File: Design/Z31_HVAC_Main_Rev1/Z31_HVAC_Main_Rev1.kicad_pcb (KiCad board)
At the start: 2 copper layers, 179 x 133.5 mm, 22 parts, among them J2 Conn_02x18_Odd_Even, J3 Conn_01x10_Male, J4 Conn_01x09_Male, U1 MEGA2560PRO, U2 MCP2515, U3 TJR1443, U4 ULN2003, U5 ULN2003, U6 ULN2003, U7 ULN2003, U8 NCV4276B, U9 ULN2003

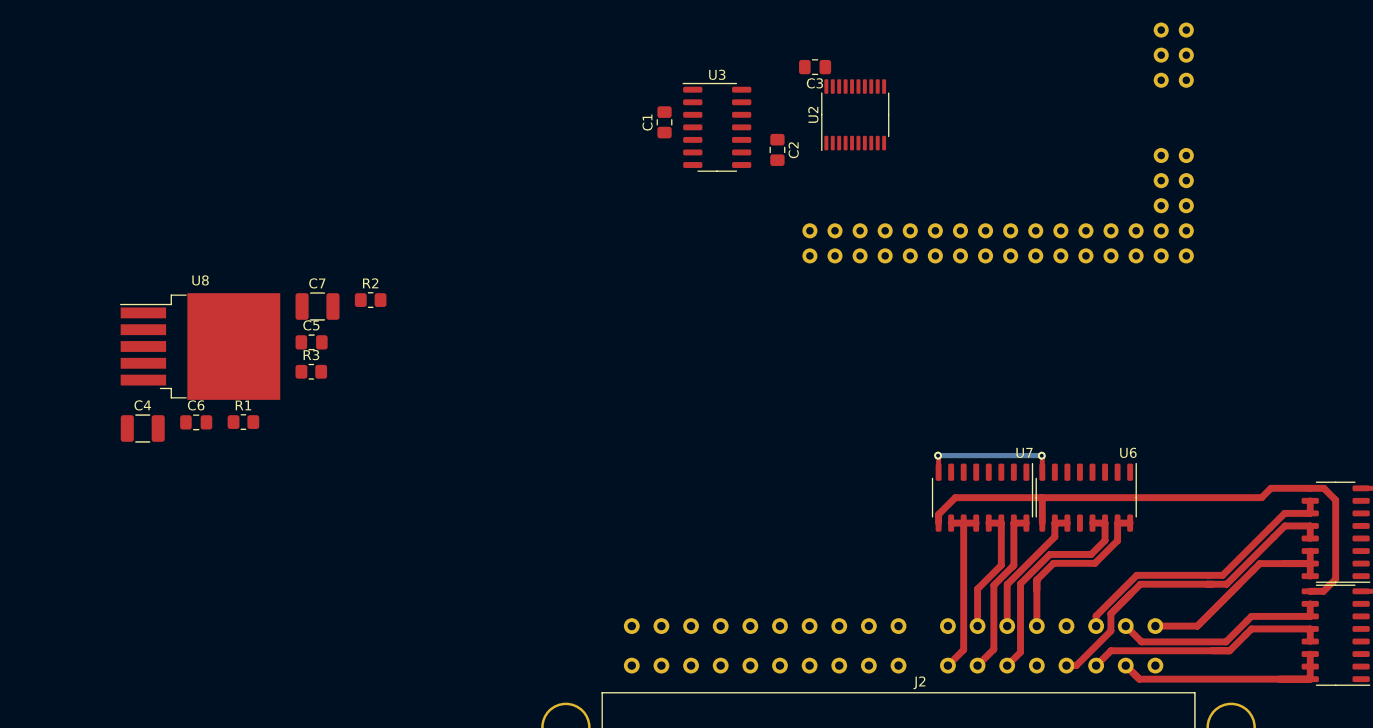
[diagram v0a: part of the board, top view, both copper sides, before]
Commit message: update to kicad-6
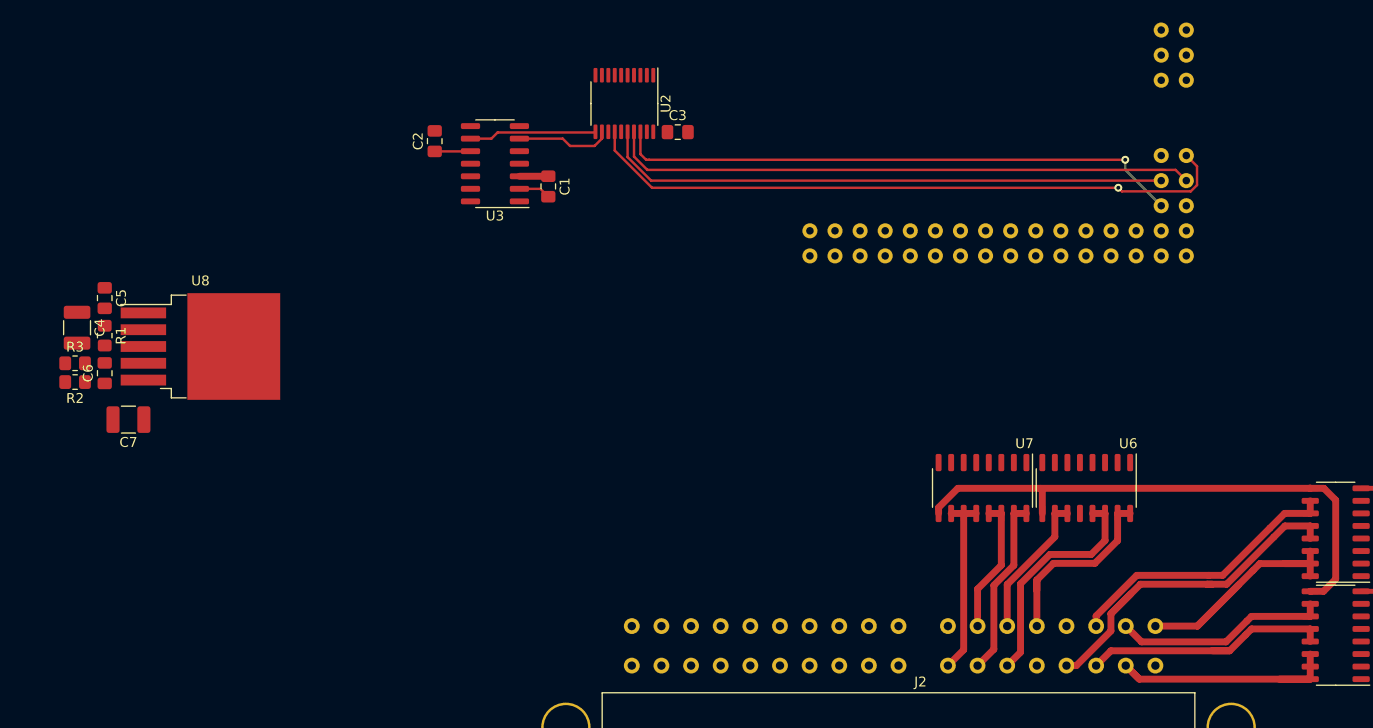
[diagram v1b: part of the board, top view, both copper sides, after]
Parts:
- moved C2 34.7 mm to (107.8, 81.9), turned to 90 degrees
- moved R2 31.0 mm to (71.4, 106.3), turned to 180 degrees
- moved R3 23.9 mm to (71.4, 104.4)
- moved U2 23.4 mm to (127.0, 78.1), turned to -90 degrees
- moved U3 22.8 mm to (113.9, 84.2), turned to 180 degrees
- moved C7 22.3 mm to (76.8, 110.1), turned to 180 degrees
- moved C5 21.4 mm to (74.4, 97.8), turned to -90 degrees
- moved R1 16.5 mm to (74.4, 101.6), turned to -90 degrees
- moved C3 15.4 mm to (132.4, 81.0), turned to 0 degrees
- moved C1 13.4 mm to (119.3, 86.5), turned to -90 degrees
- moved C4 12.2 mm to (71.6, 100.8), turned to -90 degrees
- moved C6 10.5 mm to (74.4, 105.4), turned to 90 degrees
- moved U6 0.97 mm to (173.8, 117.0)
- moved U7 0.97 mm to (163.2, 117.0)
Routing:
- net SCK: track 0.00 -> 66.4 mm, vias 0 -> 1
- net MISO: track 0.00 -> 59.4 mm
- net CS_CAN: track 0.00 -> 57.7 mm, vias 0 -> 1
- net MOSI: track 0.00 -> 57.6 mm
- net Net-(U2-Pad11): track 0.00 -> 12.9 mm
- net GND: track 28.3 -> 17.6 mm, vias 4 -> 2
- net Net-(U2-Pad12): track 0.00 -> 9.65 mm
- net Net-(C2-Pad1): track 0.00 -> 3.63 mm
- net +5V: track 0.00 -> 2.93 mm
- net /VS: track 13.7 -> 14.7 mm
- net /V3: track 22.2 -> 23.2 mm
- net /FS: track 12.7 -> 13.7 mm
- net /F3: track 17.2 -> 18.2 mm
- net /EM: track 18.6 -> 19.6 mm
- net /FR: track 17.6 -> 18.6 mm
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
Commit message: large changes
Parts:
- removed the C4 at (71.6, 100.8)
- removed the C5 at (74.4, 97.8)
- removed the U4 at (199.0, 131.9)
- added C1: 20pF, Capacitor_SMD:C_0805_2012Metric_Pad1.18x1.45mm_HandSolder, F.Cu at (136.2, 103.2)
- added C10: 100n, Capacitor_SMD:C_0805_2012Metric_Pad1.18x1.45mm_HandSolder, B.Cu at (128.6, 90.3)
- added C11: 100n, Capacitor_SMD:C_0805_2012Metric_Pad1.18x1.45mm_HandSolder, B.Cu at (128.6, 82.8)
- added C12: 100n, Capacitor_SMD:C_0805_2012Metric_Pad1.18x1.45mm_HandSolder, B.Cu at (119.5, 87.8)
- added C13: 100n, Capacitor_SMD:C_0805_2012Metric_Pad1.18x1.45mm_HandSolder, B.Cu at (119.5, 85.3)
- added C14: 100n, Capacitor_SMD:C_0805_2012Metric_Pad1.18x1.45mm_HandSolder, B.Cu at (128.5, 72.6)
- added C15: 100n, Capacitor_SMD:C_0805_2012Metric_Pad1.18x1.45mm_HandSolder, B.Cu at (119.5, 90.3)
- added C16: 100n, Capacitor_SMD:C_0805_2012Metric_Pad1.18x1.45mm_HandSolder, B.Cu at (119.5, 80.2)
- added C17: 100n, Capacitor_SMD:C_0805_2012Metric_Pad1.18x1.45mm_HandSolder, B.Cu at (128.6, 85.3)
- added C18: 100n, Capacitor_SMD:C_0805_2012Metric_Pad1.18x1.45mm_HandSolder, B.Cu at (119.5, 82.8)
- added C19: 100n, Capacitor_SMD:C_0805_2012Metric_Pad1.18x1.45mm_HandSolder, B.Cu at (128.6, 87.8)
- added C2: 20pF, Capacitor_SMD:C_0805_2012Metric_Pad1.18x1.45mm_HandSolder, F.Cu at (136.1, 96.8)
- added C20: 100n, Capacitor_SMD:C_0805_2012Metric_Pad1.18x1.45mm_HandSolder, B.Cu at (128.6, 80.2)
- added C21: 100n, Capacitor_SMD:C_0805_2012Metric_Pad1.18x1.45mm_HandSolder, B.Cu at (128.6, 77.7)
- added C22: 100n, Capacitor_SMD:C_0805_2012Metric_Pad1.18x1.45mm_HandSolder, B.Cu at (128.6, 75.2)
- added C23: 100n, Capacitor_SMD:C_0805_2012Metric_Pad1.18x1.45mm_HandSolder, B.Cu at (119.5, 72.6)
- added C24: C_Polarized, Capacitor_THT:CP_Radial_D8.0mm_P3.50mm, F.Cu at (79.8, 95.3)
- added C25: 1u, Capacitor_SMD:C_1210_3225Metric_Pad1.33x2.70mm_HandSolder, F.Cu at (84.5, 89.5)
- added C26: 100n, Capacitor_SMD:C_0805_2012Metric_Pad1.18x1.45mm_HandSolder, F.Cu at (82.8, 85.9)
- added C27: 1u, Capacitor_SMD:C_1210_3225Metric_Pad1.33x2.70mm_HandSolder, F.Cu at (215.4, 91.4)
- added C28: 100n, Capacitor_SMD:C_0805_2012Metric_Pad1.18x1.45mm_HandSolder, F.Cu at (217.1, 94.9)
- added C29: N/A, Capacitor_SMD:C_0805_2012Metric_Pad1.18x1.45mm_HandSolder, F.Cu at (91.9, 90.8)
- added C30: N/A, Capacitor_SMD:C_0805_2012Metric_Pad1.18x1.45mm_HandSolder, F.Cu at (207.9, 89.9)
- added C31: C_Small, Capacitor_SMD:C_1210_3225Metric_Pad1.33x2.70mm_HandSolder, F.Cu at (97.6, 85.3)
- added C32: C_Small, Capacitor_SMD:C_1210_3225Metric_Pad1.33x2.70mm_HandSolder, F.Cu at (203.1, 94.0)
- added C33: C_Polarized, Capacitor_SMD:CP_Elec_5x5.3, F.Cu at (101.3, 100.2)
- added C34: C_Polarized, Capacitor_SMD:CP_Elec_5x5.3, F.Cu at (187.8, 99.2)
- added C35: 100n, Capacitor_SMD:C_0805_2012Metric_Pad1.18x1.45mm_HandSolder, B.Cu at (128.5, 67.5)
- added C36: 100n, Capacitor_SMD:C_0805_2012Metric_Pad1.18x1.45mm_HandSolder, B.Cu at (128.5, 70.0)
- added C37: 100n, Capacitor_SMD:C_0805_2012Metric_Pad1.18x1.45mm_HandSolder, B.Cu at (128.5, 65.0)
- added C38: 100n, Capacitor_SMD:C_0805_2012Metric_Pad1.18x1.45mm_HandSolder, B.Cu at (128.5, 62.4)
- added C8: C, Capacitor_SMD:C_0805_2012Metric_Pad1.18x1.45mm_HandSolder, B.Cu at (119.5, 77.7)
- added C9: 100n, Capacitor_SMD:C_0805_2012Metric_Pad1.18x1.45mm_HandSolder, B.Cu at (119.5, 75.2)
- added D1: 1N4148, Diode_SMD:D_SOD-323_HandSoldering, F.Cu at (85.4, 125.5)
- added D2: 1N4148, Diode_SMD:D_SOD-323_HandSoldering, F.Cu at (90.5, 125.5)
- added D3: SMAJ18CAQ-13-F, Diode_SMD:D_SMA, F.Cu at (89.5, 115.3)
- added D4: D_Schottky, Diode_SMD:D_SMA, F.Cu at (89.5, 104.8)
- added D5: D_Schottky_Small, Diode_SMD:D_SOD-323_HandSoldering, F.Cu at (139.4, 86.0)
- added D6: D_Schottky_Small, Diode_SMD:D_SOD-323_HandSoldering, F.Cu at (139.4, 84.1)
- added F1: Polyfuse, Fuse:Fuse_1812_4532Metric_Pad1.30x3.40mm_HandSolder, F.Cu at (95.2, 114.2)
- added H1: M3, MountingHole:MountingHole_3.5mm_Pad, F.Cu at (57.5, 27.8)
- added H2: M3, MountingHole:MountingHole_3.5mm_Pad, F.Cu at (226.5, 148.2)
- added J1: Blower_Out, Connector_PinHeader_2.54mm:PinHeader_1x01_P2.54mm_Vertical, F.Cu at (159.7, 124.2)
- added J10: A_Spare_1, Connector_PinHeader_2.54mm:PinHeader_1x01_P2.54mm_Vertical, F.Cu at (116.1, 70.3)
- added J11: A_Spare_2, Connector_PinHeader_2.54mm:PinHeader_1x01_P2.54mm_Vertical, F.Cu at (116.1, 66.7)
- added J3: Conn_01x05, Personal:Z31_HVAC_Connector_1, F.Cu at (88.1, 134.6)
- added J4: Analog_En, Connector_PinHeader_2.54mm:PinHeader_1x01_P2.54mm_Vertical, F.Cu at (98.2, 81.3)
- added J5: Blower_PWM, Connector_PinHeader_2.54mm:PinHeader_1x01_P2.54mm_Vertical, F.Cu at (164.0, 70.7)
- added J6: Conn_01x03, Personal:Proto-Area, F.Cu at (196.6, 82.3)
- added J7: Conn_01x18_Male, Connector_PinHeader_2.54mm:PinHeader_1x18_P2.54mm_Vertical, F.Cu at (109.5, 40.8)
- added R10: 0R, Resistor_THT:R_Axial_DIN0204_L3.6mm_D1.6mm_P2.54mm_Vertical, F.Cu at (89.1, 52.3)
- added R11: 0R, Resistor_THT:R_Axial_DIN0204_L3.6mm_D1.6mm_P2.54mm_Vertical, F.Cu at (86.6, 52.3)
- added R12: 0R, Resistor_THT:R_Axial_DIN0204_L3.6mm_D1.6mm_P2.54mm_Vertical, F.Cu at (84.0, 52.3)
- added R13: 0R, Resistor_THT:R_Axial_DIN0204_L3.6mm_D1.6mm_P2.54mm_Vertical, F.Cu at (81.5, 52.3)
- added R14: 0R, Resistor_THT:R_Axial_DIN0204_L3.6mm_D1.6mm_P2.54mm_Vertical, F.Cu at (79.0, 52.3)
- added R15: 0R, Resistor_THT:R_Axial_DIN0204_L3.6mm_D1.6mm_P2.54mm_Vertical, F.Cu at (76.4, 52.3)
- added R16: 0R, Resistor_THT:R_Axial_DIN0204_L3.6mm_D1.6mm_P2.54mm_Vertical, F.Cu at (73.8, 52.3)
- added R17: 0R, Resistor_THT:R_Axial_DIN0204_L3.6mm_D1.6mm_P2.54mm_Vertical, F.Cu at (71.3, 52.3)
- added R18: 0R, Resistor_THT:R_Axial_DIN0204_L3.6mm_D1.6mm_P2.54mm_Vertical, F.Cu at (68.8, 52.3)
- added R19: R, Resistor_SMD:R_0805_2012Metric_Pad1.20x1.40mm_HandSolder, F.Cu at (100.1, 106.7)
- added R20: 1k, Resistor_SMD:R_0805_2012Metric_Pad1.20x1.40mm_HandSolder, F.Cu at (121.5, 109.6)
- added R21: 1k, Resistor_SMD:R_0805_2012Metric_Pad1.20x1.40mm_HandSolder, F.Cu at (118.7, 110.5)
- added R22: R_Small, Resistor_SMD:R_0805_2012Metric_Pad1.20x1.40mm_HandSolder, F.Cu at (107.5, 74.1)
- added R23: R_Small, Resistor_SMD:R_0805_2012Metric_Pad1.20x1.40mm_HandSolder, F.Cu at (109.5, 74.1)
- added R24: R_Small, Resistor_SMD:R_0805_2012Metric_Pad1.20x1.40mm_HandSolder, F.Cu at (128.7, 91.4)
- added R25: R_Small, Resistor_SMD:R_0805_2012Metric_Pad1.20x1.40mm_HandSolder, F.Cu at (128.7, 87.5)
- added R26: 1k, Resistor_SMD:R_0805_2012Metric_Pad1.20x1.40mm_HandSolder, F.Cu at (112.0, 111.3)
- added R27: 1M, Resistor_THT:R_Axial_DIN0207_L6.3mm_D2.5mm_P10.16mm_Horizontal, F.Cu at (117.2, 129.7)
- added R28: 22k, Resistor_SMD:R_0805_2012Metric_Pad1.20x1.40mm_HandSolder, F.Cu at (119.7, 96.0)
- added R29: 180k, Resistor_SMD:R_0805_2012Metric_Pad1.20x1.40mm_HandSolder, F.Cu at (121.5, 98.0)
- added R30: 1k, Resistor_SMD:R_0805_2012Metric_Pad1.20x1.40mm_HandSolder, F.Cu at (112.8, 107.2)
- added R31: 1k, Resistor_SMD:R_0805_2012Metric_Pad1.20x1.40mm_HandSolder, F.Cu at (120.2, 35.1)
- added R32: R_Small, Resistor_THT:R_Axial_DIN0207_L6.3mm_D2.5mm_P10.16mm_Horizontal, F.Cu at (123.5, 129.7)
- added R33: R_Small, Resistor_THT:R_Axial_DIN0207_L6.3mm_D2.5mm_P10.16mm_Horizontal, F.Cu at (104.5, 129.7)
- added R34: R_Small, Resistor_THT:R_Axial_DIN0207_L6.3mm_D2.5mm_P10.16mm_Horizontal, F.Cu at (114.0, 129.7)
- added R35: 1k, Resistor_SMD:R_0805_2012Metric_Pad1.20x1.40mm_HandSolder, F.Cu at (123.5, 115.9)
- added R36: 1k, Resistor_SMD:R_0805_2012Metric_Pad1.20x1.40mm_HandSolder, F.Cu at (104.5, 116.0)
- added R37: 1k, Resistor_SMD:R_0805_2012Metric_Pad1.20x1.40mm_HandSolder, F.Cu at (114.0, 115.9)
- added R38: R_Small, Resistor_THT:R_Axial_DIN0207_L6.3mm_D2.5mm_P10.16mm_Horizontal, F.Cu at (110.8, 129.7)
- added R39: R_Small, Resistor_THT:R_Axial_DIN0207_L6.3mm_D2.5mm_P10.16mm_Horizontal, F.Cu at (120.3, 129.7)
- added R4: 0R, Resistor_THT:R_Axial_DIN0204_L3.6mm_D1.6mm_P2.54mm_Vertical, F.Cu at (66.3, 47.2)
- added R40: R_Small, Resistor_THT:R_Axial_DIN0207_L6.3mm_D2.5mm_P10.16mm_Horizontal, F.Cu at (107.7, 129.7)
- added R41: 1k, Resistor_SMD:R_0805_2012Metric_Pad1.20x1.40mm_HandSolder, F.Cu at (110.8, 115.9)
- added R42: 1k, Resistor_SMD:R_0805_2012Metric_Pad1.20x1.40mm_HandSolder, F.Cu at (120.3, 115.9)
- added R43: 1k, Resistor_SMD:R_0805_2012Metric_Pad1.20x1.40mm_HandSolder, F.Cu at (107.7, 115.9)
- added R44: R_Small, Resistor_THT:R_Axial_DIN0207_L6.3mm_D2.5mm_P10.16mm_Horizontal, F.Cu at (101.4, 129.7)
- added R45: 1k, Resistor_SMD:R_0805_2012Metric_Pad1.20x1.40mm_HandSolder, F.Cu at (101.4, 116.0)
- added R46: 10k, Resistor_SMD:R_0805_2012Metric_Pad1.20x1.40mm_HandSolder, F.Cu at (88.0, 89.7)
- added R47: 10k, Resistor_SMD:R_0805_2012Metric_Pad1.20x1.40mm_HandSolder, F.Cu at (211.9, 91.1)
- added R48: N/A, Resistor_SMD:R_0805_2012Metric_Pad1.20x1.40mm_HandSolder, F.Cu at (91.9, 88.8)
- added R49: N/A, Resistor_SMD:R_0805_2012Metric_Pad1.20x1.40mm_HandSolder, F.Cu at (91.9, 92.8)
- added R5: 0R, Resistor_THT:R_Axial_DIN0204_L3.6mm_D1.6mm_P2.54mm_Vertical, F.Cu at (101.8, 46.2)
- added R50: N/A, Resistor_SMD:R_0805_2012Metric_Pad1.20x1.40mm_HandSolder, F.Cu at (208.0, 91.9)
- added R51: N/A, Resistor_SMD:R_0805_2012Metric_Pad1.20x1.40mm_HandSolder, F.Cu at (208.0, 87.9)
- added R52: R_Small, Resistor_SMD:R_0805_2012Metric_Pad1.20x1.40mm_HandSolder, F.Cu at (144.2, 117.7)
- added R53: R_Small, Resistor_SMD:R_0805_2012Metric_Pad1.20x1.40mm_HandSolder, F.Cu at (138.5, 117.7)
- added R54: R_Small, Resistor_SMD:R_0805_2012Metric_Pad1.20x1.40mm_HandSolder, F.Cu at (140.5, 121.7)
- added R55: R_Small, Resistor_SMD:R_0805_2012Metric_Pad1.20x1.40mm_HandSolder, F.Cu at (138.5, 119.7)
- added R56: R_Small, Resistor_SMD:R_0805_2012Metric_Pad1.20x1.40mm_HandSolder, F.Cu at (141.3, 116.7)
- added R57: R_Small, Resistor_SMD:R_0805_2012Metric_Pad1.20x1.40mm_HandSolder, F.Cu at (136.8, 121.7)
- added R58: 100R, Resistor_SMD:R_0805_2012Metric_Pad1.20x1.40mm_HandSolder, F.Cu at (133.6, 89.1)
- added R59: R_Small, Resistor_SMD:R_0805_2012Metric_Pad1.20x1.40mm_HandSolder, F.Cu at (144.2, 114.5)
- added R6: 0R, Resistor_THT:R_Axial_DIN0204_L3.6mm_D1.6mm_P2.54mm_Vertical, F.Cu at (99.3, 46.2)
- added R60: R_Small, Resistor_SMD:R_0805_2012Metric_Pad1.20x1.40mm_HandSolder, F.Cu at (133.6, 119.7)
- added R61: 4k7, Resistor_SMD:R_0805_2012Metric_Pad1.20x1.40mm_HandSolder, F.Cu at (139.4, 88.1)
- added R62: R_Small, Resistor_SMD:R_0805_2012Metric_Pad1.20x1.40mm_HandSolder, F.Cu at (130.6, 118.7)
- added R63: R_Small, Resistor_SMD:R_0805_2012Metric_Pad1.20x1.40mm_HandSolder, F.Cu at (144.2, 112.6)
- added R64: R_Small, Resistor_SMD:R_0805_2012Metric_Pad1.20x1.40mm_HandSolder, F.Cu at (142.2, 110.6)
- added R65: R_Small, Resistor_SMD:R_0805_2012Metric_Pad1.20x1.40mm_HandSolder, F.Cu at (131.5, 112.6)
- added R7: 0R, Resistor_THT:R_Axial_DIN0204_L3.6mm_D1.6mm_P2.54mm_Vertical, F.Cu at (96.8, 46.2)
- added R8: 0R, Resistor_THT:R_Axial_DIN0204_L3.6mm_D1.6mm_P2.54mm_Vertical, F.Cu at (94.2, 46.2)
- added R9: 0R, Resistor_THT:R_Axial_DIN0204_L3.6mm_D1.6mm_P2.54mm_Vertical, F.Cu at (91.6, 52.3)
- added TH1: Thermistor, Resistor_SMD:R_0805_2012Metric_Pad1.20x1.40mm_HandSolder, F.Cu at (103.0, 105.7)
- added U10: ULN2003, Package_SO:SO-16_3.9x9.9mm_P1.27mm, F.Cu at (198.9, 131.9)
- added U11: NCV4276B, Package_TO_SOT_SMD:TO-263-5_TabPin3, F.Cu at (89.5, 79.4)
- added U12: NCV4276B, Package_TO_SOT_SMD:TO-263-5_TabPin3, F.Cu at (210.4, 101.4)
- added U9: ULN2003, Package_SO:SO-16_3.9x9.9mm_P1.27mm, F.Cu at (198.9, 121.5)
- added Y1: 8MHz, Crystal:Crystal_SMD_HC49-SD, F.Cu at (139.8, 99.9)
- C6: value N/A -> 100pF
- C7: value C_Small -> 100pF; footprint Capacitor_SMD:C_1210_3225Metric_Pad1.33x2.70mm_HandSolder -> Capacitor_SMD:C_0805_2012Metric_Pad1.18x1.45mm_HandSolder
- J2: footprint Personal:z31_hvac_connector_2 -> Personal:TE-172023
- R1: value 10k -> R_Small
- R2: value N/A -> R_Small
- R3: value N/A -> 100R; footprint Resistor_SMD:R_0805_2012Metric_Pad1.20x1.40mm_HandSolder -> Resistor_THT:R_Axial_DIN0207_L6.3mm_D2.5mm_P7.62mm_Horizontal
- U3: renamed from U1; moved to F.Cu
- U5: value ULN2003 -> LM358; footprint Package_SO:SO-16_3.9x9.9mm_P1.27mm -> Package_SO:SO-8_5.3x6.2mm_P1.27mm
- U8: value NCV4276B -> ULN2003; footprint Package_TO_SOT_SMD:TO-263-5_TabPin3 -> Package_SO:SO-16_3.9x9.9mm_P1.27mm
- moved C7 148.7 mm to (220.5, 148.2)
- moved U8 101.2 mm to (184.3, 117.1), turned to -90 degrees
- moved R1 83.0 mm to (154.1, 124.9), turned to 90 degrees
- moved R2 81.7 mm to (151.2, 123.9)
- moved U5 80.3 mm to (120.6, 103.8), turned to -90 degrees
- moved C6 73.4 mm to (57.5, 34.0), turned to -90 degrees
- moved R3 58.9 mm to (114.9, 144.2), turned to 180 degrees
- moved C4 58.8 mm to (151.0, 121.9), turned to 180 degrees
- moved U2 51.3 mm to (153.3, 117.1), turned to -90 degrees
- moved C5 37.6 mm to (154.5, 111.4), turned to 90 degrees
- moved U1 29.2 mm to (146.9, 99.4), turned to 90 degrees
- moved C3 25.2 mm to (143.4, 93.6), turned to 90 degrees
- moved U3 19.3 mm to (140.5, 76.4), turned to 90 degrees
- moved U6 10.5 mm to (163.2, 117.1)
- moved U7 10.5 mm to (173.7, 117.1)
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- renumbered C1 to C3, C2 to C4, C3 to C5, J3 to J8, J4 to J9, U2 to U1, U3 to U2, U9 to U4
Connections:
- net Net-(U2-Pad1) renamed /TXCAN
- net Net-(U2-Pad2) renamed /RXCAN
- C4 pad 1: Net-(C2-Pad1) -> +12V
- C6 pad 1: +5VA -> Net-(C6-Pad1)
- C6 pad 2: Net-(C6-Pad2) -> GND
- C7 pad 1: +5VA -> Net-(C7-Pad1)
- J2 pad 10: unconnected-(J2-Pad10) -> /A3
- J2 pad 2: unconnected-(J2-Pad2) -> /A1
- J2 pad 7: unconnected-(J2-Pad7) -> /A2
- J8 pad 1: /Illum_A -> /L2
- J8 pad 2: /Illum_B -> /L1
- J9 pad 1: LED_Supply -> +12V
- R1 pad 1: /EN_ANALOG -> /+12V_Ignition
- R1 pad 2: GND -> Net-(R1-Pad2)
- R2 pad 1: +5VA -> Net-(R1-Pad2)
- R2 pad 2: Net-(C6-Pad2) -> GND
- R3 pad 1: Net-(C6-Pad2) -> /+12V_Ignition
- R3 pad 2: GND -> Net-(D1-Pad1)
- U1 pad 11: Net-(U2-Pad11) -> /TRJ1443_STB
- U1 pad 12: Net-(U2-Pad12) -> /TRJ1443EN
- U1 pad 13: unconnected-(U2-Pad13) -> /INT_CAN
- U1 pad 19: unconnected-(U2-Pad19) -> /RESET_CAN
- U1 pad 4: unconnected-(U2-Pad4) -> /TRJ1443ERR
- U1 pad 8: unconnected-(U2-Pad8) -> Net-(C1-Pad2)
- U1 pad 9: unconnected-(U2-Pad9) -> Net-(C2-Pad2)
- U2 pad 10: Net-(C2-Pad1) -> +12V
- U2 pad 14: unconnected-(U3-Pad14) -> /TRJ1443EN
- U2 pad 6: Net-(U2-Pad12) -> /TRJ1443_STB
- U2 pad 7: unconnected-(U3-Pad7) (its old number) -> /REG_INHIBIT
- U2 pad 8: unconnected-(U3-Pad8) (its old number) -> /TRJ1443ERR
- U2 pad 9: Net-(U2-Pad11) -> Net-(R1-Pad2)
- U3 pad 10: +5VA -> unconnected-(U3-Pad10)
- U3 pad 13: unconnected-(U1-Pad13) -> /Fan_Relay
- U3 pad 14: unconnected-(U1-Pad14) -> /SV5_Air_Mix_Door_2
- U3 pad 15: unconnected-(U1-Pad15) (its old number) -> /SV4_Air_Mix_Door_2
- U3 pad 16: unconnected-(U1-Pad16) -> /SV9_Air_Mix_Door_1
- U3 pad 17: unconnected-(U1-Pad17) -> /SV8_Air_Mix_Door_1
- U3 pad 18: unconnected-(U1-Pad18) -> /Manual_Defrost_AC
- U3 pad 19: unconnected-(U1-Pad19) -> /Aux_3
- U3 pad 20: unconnected-(U1-Pad20) -> /Aux_2
- U3 pad 21: unconnected-(U1-Pad21) -> /SV6_Vent_Door_2
- U3 pad 22: unconnected-(U1-Pad22) -> /SV2_Intake_Door_1
- U3 pad 23: unconnected-(U1-Pad23) -> /SV7_Floor_Door
- U3 pad 24: unconnected-(U1-Pad24) -> /Blower_Speed
- U3 pad 25: unconnected-(U1-Pad25) -> /SV3_Intake_Door_3
- U3 pad 26: unconnected-(U1-Pad26) -> /Water_Cock
- U3 pad 27: unconnected-(U1-Pad27) -> /Compressor_Relay
- U3 pad 28: unconnected-(U1-Pad28) -> /Aux_1
- U3 pad 29: unconnected-(U1-Pad29) -> Net-(U3-Pad29)
- U3 pad 3: unconnected-(U1-Pad3) (its old number) -> GND
- U3 pad 30: unconnected-(U1-Pad30) -> /INT_CAN
- U3 pad 31: unconnected-(U1-Pad31) -> Net-(U3-Pad31)
- U3 pad 32: unconnected-(U1-Pad32) -> /Key_Row_4
- U3 pad 33: unconnected-(U1-Pad33) -> Net-(U3-Pad33)
- U3 pad 34: unconnected-(U1-Pad34) -> /Key_Col_2
- U3 pad 35: unconnected-(U1-Pad35) -> Net-(U3-Pad35)
- U3 pad 36: unconnected-(U1-Pad36) -> /Key_Row_3
- U3 pad 37: unconnected-(U1-Pad37) -> Net-(U3-Pad37)
- U3 pad 38: unconnected-(U1-Pad38) -> /Key_Col_1
- U3 pad 39: unconnected-(U1-Pad39) -> Net-(U3-Pad39)
- U3 pad 4: unconnected-(U1-Pad4) -> GND
- U3 pad 40: unconnected-(U1-Pad40) -> /Key_Row_2
- U3 pad 41: unconnected-(U1-Pad41) -> Net-(U3-Pad41)
- U3 pad 42: unconnected-(U1-Pad42) -> /Key_Row_1
- U3 pad 49: unconnected-(U1-Pad49) -> /Signal_In (Analog)/Temp_In_Lower
- U3 pad 5: unconnected-(U1-Pad5) (its old number) -> +5V
- U3 pad 50: unconnected-(U1-Pad50) -> /Signal_In (Analog)/Lighting_Low
- U3 pad 51: unconnected-(U1-Pad51) -> /Signal_In (Analog)/Sun Load
- U3 pad 52: unconnected-(U1-Pad52) -> /Signal_In (Analog)/Temp_In_Upper
- U3 pad 53: unconnected-(U1-Pad53) -> /Signal_In (Analog)/Position_2
- U3 pad 54: unconnected-(U1-Pad54) -> /Signal_In (Analog)/Temp_Water
- U3 pad 55: unconnected-(U1-Pad55) -> /Signal_In (Analog)/Temp_Duct_Lower
- U3 pad 56: unconnected-(U1-Pad56) -> /Signal_In (Analog)/Position_1
- U3 pad 57: unconnected-(U1-Pad57) -> /Signal_In (Analog)/Temp_Ambient
- U3 pad 58: unconnected-(U1-Pad58) -> /Signal_In (Analog)/Temp_Duct_Upper
- U3 pad 59: unconnected-(U1-Pad59) -> /Signal_In (Analog)/Temp_Module
- U3 pad 6: unconnected-(U1-Pad6) (its old number) -> +5V
- U3 pad 60: unconnected-(U1-Pad60) -> /Signal_In (Analog)/Temp_Duct_Defrost
- U3 pad 61: unconnected-(U1-Pad61) -> /Signal_In (Analog)/Battery_Voltage
- U3 pad 62: unconnected-(U1-Pad62) -> /Signal_In (Analog)/A_Spare_1
- U3 pad 63: unconnected-(U1-Pad63) -> /Signal_In (Analog)/A_Spare_2
- U3 pad 64: unconnected-(U1-Pad64) -> /Signal_In (Analog)/Position_Split
- U3 pad 65: unconnected-(U1-Pad65) -> /DAux1
- U3 pad 66: unconnected-(U1-Pad66) -> /Singal_In (Discrete)/Signal_Lighting
- U3 pad 67: unconnected-(U1-Pad67) -> /DAux2
- U3 pad 68: unconnected-(U1-Pad68) -> /Singal_In (Discrete)/Superheat_Timer
- U3 pad 69: unconnected-(U1-Pad69) -> /DAux3
- U3 pad 70: unconnected-(U1-Pad70) -> /Singal_In (Discrete)/Bulb_Check
- U3 pad 71: unconnected-(U1-Pad71) -> /DSC1
- U3 pad 72: unconnected-(U1-Pad72) -> /Ignition
- U3 pad 73: unconnected-(U1-Pad73) -> /DCS2
- U3 pad 74: unconnected-(U1-Pad74) -> /Singal_In (Discrete)/OneWire
- U3 pad 75: unconnected-(U1-Pad75) -> /DCS3
- U3 pad 76: unconnected-(U1-Pad76) -> /RESET_CAN
- U3 pad 77: unconnected-(U1-Pad77) -> /BL1
- U3 pad 78: unconnected-(U1-Pad78) -> /BL2
- U3 pad 79: unconnected-(U1-Pad79) -> /BL3
- U3 pad 80: unconnected-(U1-Pad80) -> RST
- U3 pad 84: unconnected-(U1-Pad84) -> D/C
- U4 pad 1: unconnected-(U9-Pad1) -> Net-(U3-Pad29)
- U4 pad 2: unconnected-(U9-Pad2) -> Net-(U3-Pad31)
- U4 pad 3: unconnected-(U9-Pad3) -> Net-(U3-Pad33)
- U4 pad 4: unconnected-(U9-Pad4) -> Net-(U3-Pad35)
- U4 pad 5: unconnected-(U9-Pad5) -> Net-(U3-Pad37)
- U4 pad 6: unconnected-(U9-Pad6) -> Net-(U3-Pad39)
- U4 pad 7: unconnected-(U9-Pad7) -> Net-(U3-Pad41)
- U4 pad 8: unconnected-(U9-Pad8) -> GND
- U5 pad 1: /Water_Cock -> /Signal_In (Analog)/Sun Load
- U5 pad 2: /Water_Cock -> Net-(R28-Pad1)
- U5 pad 3: /Water_Cock -> /ZC
- U5 pad 4: /SV6_Vent_Door_2 -> GND
- U5 pad 5: /SV6_Vent_Door_2 -> Net-(R20-Pad1)
- U5 pad 6: /SV2_Intake_Door_1 -> Net-(U5-Pad6)
- U5 pad 7: /SV2_Intake_Door_1 -> Net-(U5-Pad6)
- U5 pad 8: GND -> +5VA
- U6 pad 1: /Manual_Defrost_AC -> /SV4_Air_Mix_Door_2
- U6 pad 10: /VS -> /FR
- U6 pad 11: /VS -> /FR
- U6 pad 12: unconnected-(U6-Pad12) -> /FR
- U6 pad 13: /V3 -> /FS
- U6 pad 14: /V3 -> /FS
- U6 pad 15: /EM -> /F3
- U6 pad 16: /EM -> /F3
- U6 pad 2: /Manual_Defrost_AC -> /SV4_Air_Mix_Door_2
- U6 pad 3: /SV8_Air_Mix_Door_1 -> /SV5_Air_Mix_Door_2
- U6 pad 4: /SV8_Air_Mix_Door_1 -> /SV5_Air_Mix_Door_2
- U6 pad 5: GND -> /Fan_Relay
- U6 pad 6: /SV9_Air_Mix_Door_1 -> /Fan_Relay
- U6 pad 7: /SV9_Air_Mix_Door_1 -> /Fan_Relay
- U6 pad 9: +12V_Battery -> +12V
- U7 pad 1: /SV4_Air_Mix_Door_2 -> /Manual_Defrost_AC
- U7 pad 10: /FR -> /VS
- U7 pad 11: /FR -> /VS
- U7 pad 12: /FR -> unconnected-(U7-Pad12)
- U7 pad 13: /FS -> /V3
- U7 pad 14: /FS -> /V3
- U7 pad 15: /F3 -> /EM
- U7 pad 16: /F3 -> /EM
- U7 pad 2: /SV4_Air_Mix_Door_2 -> /Manual_Defrost_AC
- U7 pad 3: /SV5_Air_Mix_Door_2 -> /SV8_Air_Mix_Door_1
- U7 pad 4: /SV5_Air_Mix_Door_2 -> /SV8_Air_Mix_Door_1
- U7 pad 5: /Fan_Relay -> GND
- U7 pad 6: /Fan_Relay -> /SV9_Air_Mix_Door_1
- U7 pad 7: /Fan_Relay -> /SV9_Air_Mix_Door_1
- U7 pad 9: +12V_Battery -> +12V
- U8 pad 1: Net-(C4-Pad1) -> GND
- U8 pad 2: /EN_ANALOG -> /SV6_Vent_Door_2
- U8 pad 3: GND -> /SV6_Vent_Door_2
- U8 pad 4: Net-(C6-Pad2) -> /Aux_2
- U8 pad 5: +5VA -> /Aux_2
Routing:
- net +12V: track 0.00 -> 531.7 mm, vias 0 -> 4
- net +5V: track 2.93 -> 280.0 mm, vias 0 -> 7
- net +5VA: track 0.00 -> 251.9 mm, vias 0 -> 1
- net /L1: track 0.00 -> 151.0 mm, vias 0 -> 4
- net /L2: track 0.00 -> 149.9 mm, vias 0 -> 2
- net GND: track 17.6 -> 134.7 mm, vias 2 -> 161
- net /Aux_1: track 0.00 -> 108.1 mm
- net /Compressor_Relay: track 0.00 -> 107.4 mm
- net /SV3_Intake_Door_3: track 0.00 -> 100.4 mm
- net /Water_Cock: track 0.00 -> 93.0 mm, vias 0 -> 1
- net /SV7_Floor_Door: track 0.00 -> 89.1 mm
- net /REG_INHIBIT: track 0.00 -> 87.8 mm, vias 0 -> 2
- net /+12V_Ignition: track 0.00 -> 83.1 mm, vias 0 -> 2
- net /SV2_Intake_Door_1: track 0.00 -> 81.6 mm
- net /Singal_In (Discrete)/Superheat_Timer: track 0.00 -> 75.9 mm
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- added copper zone on B.Cu, net GND
- added copper zone on F.Cu, net GND
- added copper zone on F.Cu, net Net-(D3-Pad2)
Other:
- outline, holes or cut-outs redrawn
- board text added: "+12V"
- board text added: "+5V"
- board text added: "Aux1"
- board text added: "Aux2"
- board text added: "Aux3"
- board text added: "CANH"
- board text added: "CANL"
- board text added: "CR"
- board text added: "DD"
- board text added: "DL"
- board text added: "DU"
- board text added: "EM"
- board text added: "F3"
- board text added: "FL"
- board text added: "FR"
- board text added: "FS"
- board text added: "GA"
- board text added: "GND"
- board text added: "I1"
- board text added: "I2"
- board text added: "L1"
- board text added: "L2"
- board text added: "LA"
- board text added: "LC"
- board text added: "OneWire"
- board text added: "PL"
- board text added: "PU"
- board text added: "SL"
- board text added: "Sunload"
- board text added: "TA"
- board text added: "TL"
- board text added: "TU"
- board text added: "TW"
- board text added: "Temp-Ambient"
- board text added: "Temp-Defrost"
- board text added: "Temp-Duct-Hi"
- board text added: "Temp-Duct-Lo"
- board text added: "Temp-Hi"
- board text added: "Temp-Lo"
- board text added: "Temp-Water"
- board text added: "V2"
- board text added: "V3"
- board text added: "VA"
- board text added: "VB"
- board text added: "VF"
- board text added: "VS"
- board text added: "WC"
- board text added: "Z31-HVAC-Main-Rev 1 A.M. 2022"
- board text added: "ZC"
